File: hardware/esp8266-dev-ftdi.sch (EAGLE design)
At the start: 56 parts, among them CON1 USBMICRO-NO_CENTER-LONG_PADS

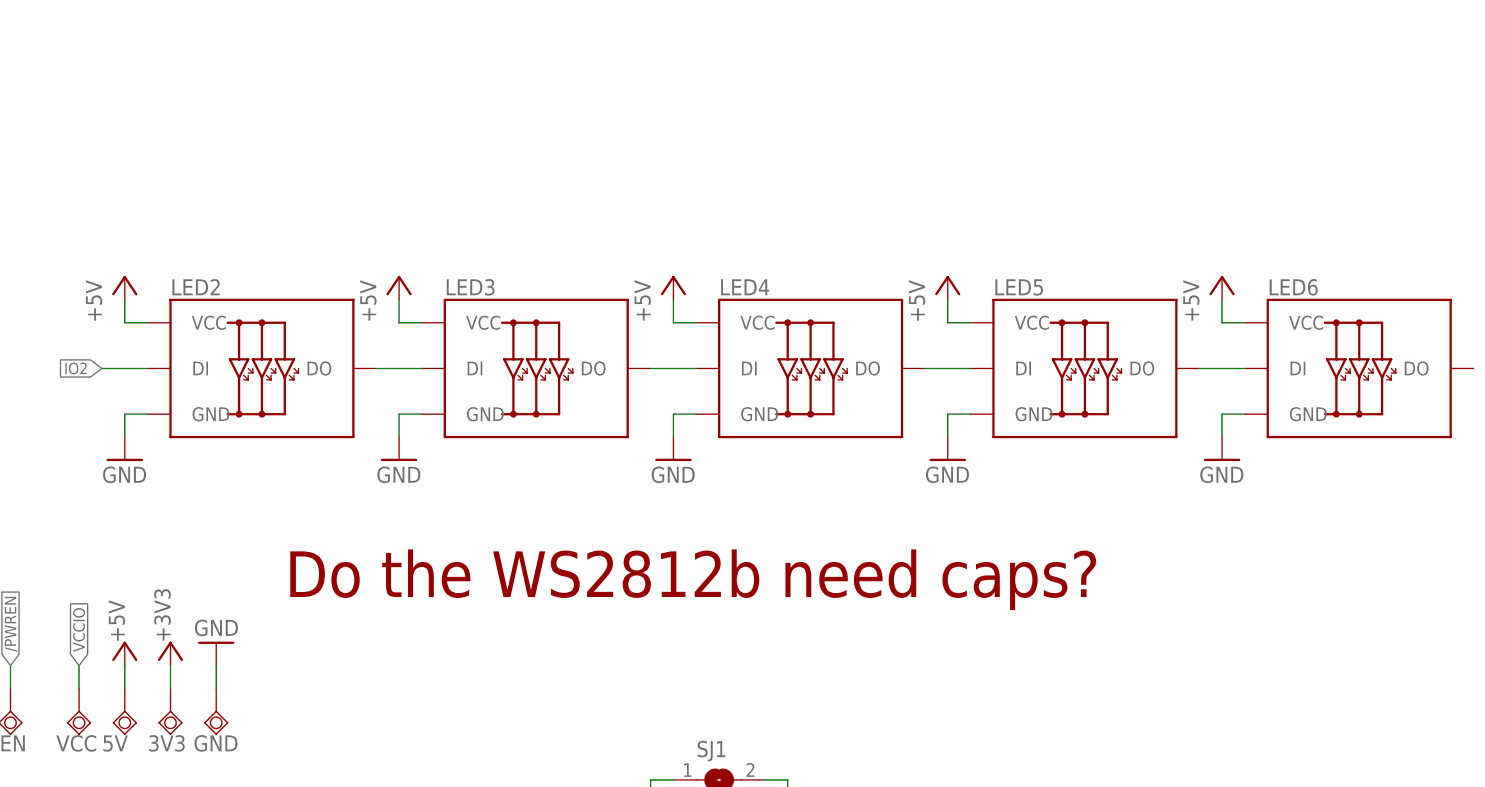
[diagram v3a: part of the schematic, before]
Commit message: added decoupling caps for leds
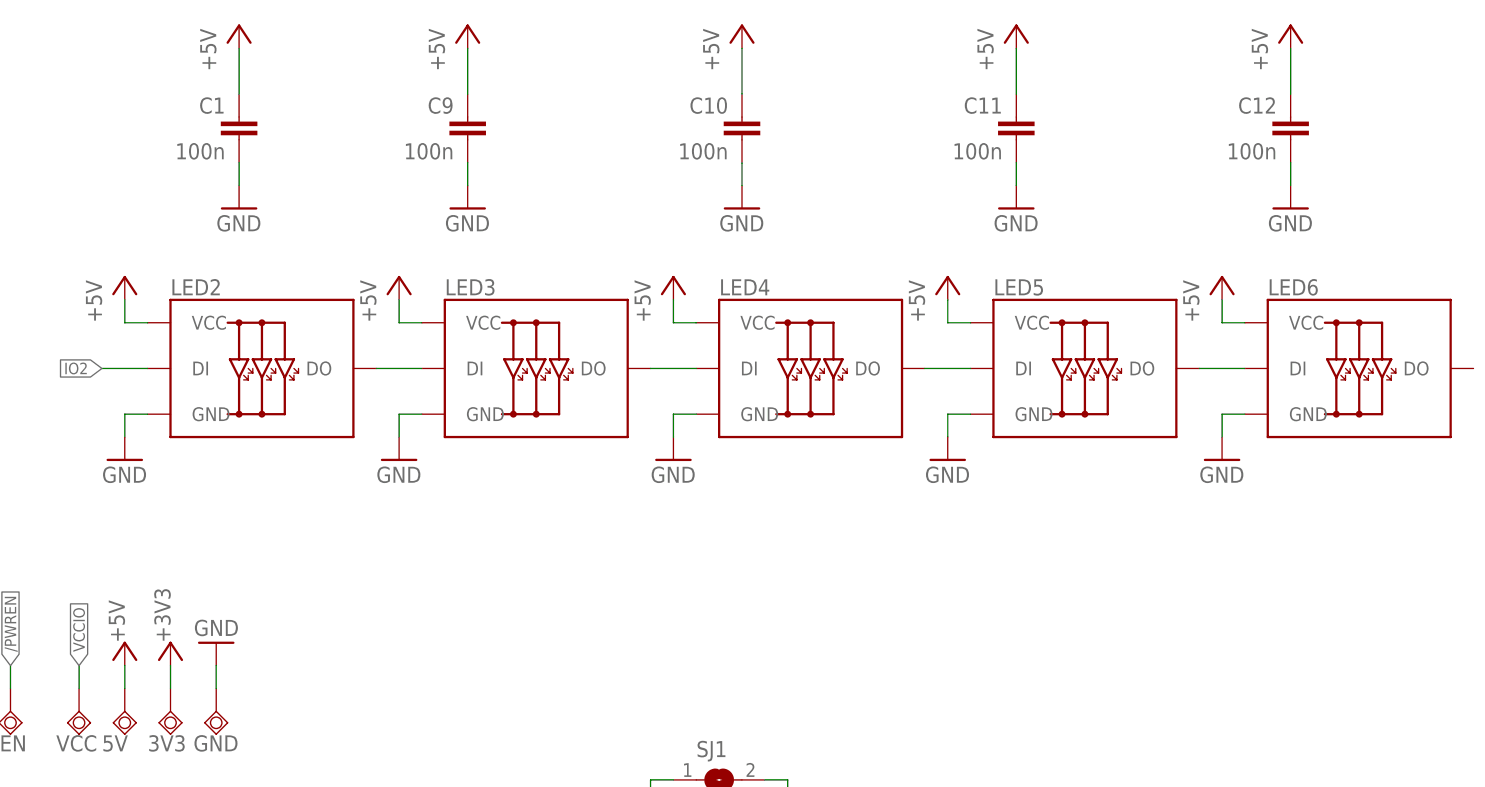
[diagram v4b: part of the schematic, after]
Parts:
- added C1, C10, C11, C12, C9: 100n, p.peter-rcl:C-EUC0805
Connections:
- net +5V: now also C1.1, C10.1, C11.1, C12.1, C9.1
- net GND: now also C1.2, C10.2, C11.2, C12.2, C9.2
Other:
- note removed: "Do the WS2812b need caps?"
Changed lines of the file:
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@@
 <part name="R13" library="p.peter-rcl" deviceset="R-EU_" device="R0805" value="540"/>
 <part name="LED-TX1" library="p.peter-leds" deviceset="LED" device="0805"/>
+<part name="C1" library="p.peter-rcl" deviceset="C-EU" device="C0805" value="100n"/>
+<part name="P+14" library="supply1" deviceset="+5V" device=""/>
+<part name="GND25" library="supply1" deviceset="GND" device=""/>
+<part name="C9" library="p.peter-rcl" deviceset="C-EU" device="C0805" value="100n"/>
+<part name="P+15" library="supply1" deviceset="+5V" device=""/>
+<part name="GND26" library="supply1" deviceset="GND" device=""/>
+<part name="C10" library="p.peter-rcl" deviceset="C-EU" device="C0805" value="100n"/>
+<part name="P+16" library="supply1" deviceset="+5V" device=""/>
+<part name="GND27" library="supply1" deviceset="GND" device=""/>
+<part name="C11" library="p.peter-rcl" deviceset="C-EU" device="C0805" value="100n"/>
+<part name="P+17" library="supply1" deviceset="+5V" device=""/>
+<part name="GND28" library="supply1" deviceset="GND" device=""/>
+<part name="C12" library="p.peter-rcl" deviceset="C-EU" device="C0805" value="100n"/>
+<part name="P+18" library="supply1" deviceset="+5V" device=""/>
+<part name="GND29" library="supply1" deviceset="GND" device=""/>
 </parts>
 <sheets>
@@
 v0.1 (8e144a9ffe)
 </text>
-<text x="86.36" y="83.82" size="5.08" layer="94">Do the WS2812b need caps?</text>
 </plain>
 <instances>
@@
 <instance part="R13" gate="G$1" x="109.22" y="-66.04" rot="MR0"/>
 <instance part="LED-TX1" gate="G$1" x="119.38" y="-66.04"/>
+<instance part="C1" gate="G$1" x="81.28" y="137.16" rot="MR0"/>
+<instance part="P+14" gate="1" x="81.28" y="147.32"/>
+<instance part="GND25" gate="1" x="81.28" y="127"/>
+<instance part="C9" gate="G$1" x="106.68" y="137.16" rot="MR0"/>
+<instance part="P+15" gate="1" x="106.68" y="147.32"/>
+<instance part="GND26" gate="1" x="106.68" y="127"/>
+<instance part="C10" gate="G$1" x="137.16" y="137.16" rot="MR0"/>
+<instance part="P+16" gate="1" x="137.16" y="147.32"/>
+<instance part="GND27" gate="1" x="137.16" y="127"/>
+<instance part="C11" gate="G$1" x="167.64" y="137.16" rot="MR0"/>
+<instance part="P+17" gate="1" x="167.64" y="147.32"/>
+<instance part="GND28" gate="1" x="167.64" y="127"/>
+<instance part="C12" gate="G$1" x="198.12" y="137.16" rot="MR0"/>
+<instance part="P+18" gate="1" x="198.12" y="147.32"/>
+<instance part="GND29" gate="1" x="198.12" y="127"/>
 </instances>
 <busses>
@@
 <pinref part="GND" gate="G$1" pin="TP"/>
 </segment>
+<segment>
+<pinref part="C1" gate="G$1" pin="2"/>
+<pinref part="GND25" gate="1" pin="GND"/>
+<wire x1="81.28" y1="132.08" x2="81.28" y2="129.54" width="0.1524" layer="91"/>
+</segment>
+<segment>
+<pinref part="C9" gate="G$1" pin="2"/>
+<pinref part="GND26" gate="1" pin="GND"/>
+<wire x1="106.68" y1="132.08" x2="106.68" y2="129.54" width="0.1524" layer="91"/>
+</segment>
+<segment>
+<pinref part="C10" gate="G$1" pin="2"/>
+<pinref part="GND27" gate="1" pin="GND"/>
+<wire x1="137.16" y1="132.08" x2="137.16" y2="129.54" width="0.1524" layer="91"/>
+</segment>
+<segment>
+<pinref part="C11" gate="G$1" pin="2"/>
+<pinref part="GND28" gate="1" pin="GND"/>
+<wire x1="167.64" y1="132.08" x2="167.64" y2="129.54" width="0.1524" layer="91"/>
+</segment>
+<segment>
+<pinref part="C12" gate="G$1" pin="2"/>
+<pinref part="GND29" gate="1" pin="GND"/>
+<wire x1="198.12" y1="132.08" x2="198.12" y2="129.54" width="0.1524" layer="91"/>
+</segment>
 </net>
 <net name="+5V" class="0">
@@
 <pinref part="5V" gate="G$1" pin="TP"/>
 </segment>
+<segment>
+<pinref part="C1" gate="G$1" pin="1"/>
+<pinref part="P+14" gate="1" pin="+5V"/>
+<wire x1="81.28" y1="144.78" x2="81.28" y2="139.7" width="0.1524" layer="91"/>
+</segment>
+<segment>
+<pinref part="C9" gate="G$1" pin="1"/>
+<pinref part="P+15" gate="1" pin="+5V"/>
+<wire x1="106.68" y1="144.78" x2="106.68" y2="139.7" width="0.1524" layer="91"/>
+</segment>
+<segment>
+<pinref part="C10" gate="G$1" pin="1"/>
+<pinref part="P+16" gate="1" pin="+5V"/>
+<wire x1="137.16" y1="144.78" x2="137.16" y2="139.7" width="0.1524" layer="91"/>
+</segment>
+<segment>
+<pinref part="C11" gate="G$1" pin="1"/>
+<pinref part="P+17" gate="1" pin="+5V"/>
+<wire x1="167.64" y1="144.78" x2="167.64" y2="139.7" width="0.1524" layer="91"/>
+</segment>
+<segment>
+<pinref part="C12" gate="G$1" pin="1"/>
+<pinref part="P+18" gate="1" pin="+5V"/>
+<wire x1="198.12" y1="144.78" x2="198.12" y2="139.7" width="0.1524" layer="91"/>
+</segment>
 </net>

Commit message: cleanup schematict
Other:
- note added: "ESP 8266 development board https://github.com/JustgeekDE /ESP8266-devBoard v0.1 (15b41cca75)"
- note added: "LEDs"
- note added: "Serial to USB"
- note removed: "ESP 8266 development board https://github.com/JustgeekDE /ESP8266-devBoard v0.1 (8e144a9ffe)"
- moved on the sheet: C1, C10, C11, C12, C2, C3, C4, C5, C6, C7, C8, C9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
